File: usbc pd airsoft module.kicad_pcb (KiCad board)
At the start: 2 copper layers, 135 x 21 mm, 102 parts, among them J1 USB_C_Receptacle_USB2.0_16P, J2 BALANCE 3S (JST-XH 4P), Q1 2N7002, Q2 DMP3099L, Q3 2N7002, U1 CH224K, U2 TPD2E2U06DCK, U3 BQ25798RQMR, U4 BQ7692003PWR, U5 AP7381-33SA-7, U6 STM32F042F6P6

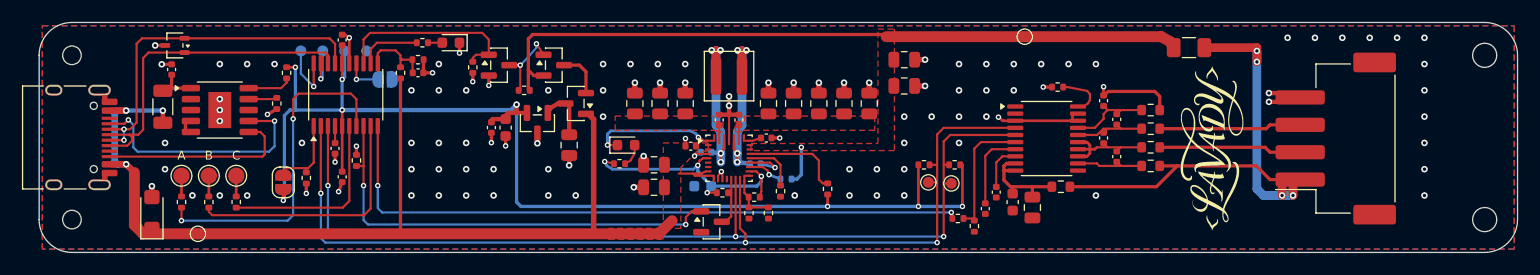
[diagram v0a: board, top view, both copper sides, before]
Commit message: Strap notches in both long edges, via-free back text, regenerated production files
- 4 U-notches (3.8 mm wide, 1.5 mm deep, rounded) at x 137.1 / 173.5, straight across
  from each other (21.0 mm centre to centre), so a strap can hold the 20.5 mm pack
  without sliding (layout_work/regionH.py).
- Copper kept >= 0.3 mm from the notches: bottom bus lanes packed upward (CHG_EN 117.9,
  SCL 118.45, SDA 119.0; I2C steps back down at the U3 tee-in), VBUS steps up past the
  x 137 notch, PWR_HOLD dips past it, R26/D4 to y 102.75, R23/C35 to y 106.3/107.3,
  BAT_P edge track dips at x 173.
- Back text '<desighned by Fluff>' moved by the user to x 125-152; vias kept off it
  (no stitching there, U6 fan-out vias to y 116.0, C29/C32/C34 GND vias moved).
- DRC 0 errors / 0 unconnected / schematic parity 0.
- Gerbers, drill, BOM, pick-and-place, assembly PDFs and zips regenerated.

Co-Authored-By: Claude Opus 5.5 <noreply@anthropic.com>
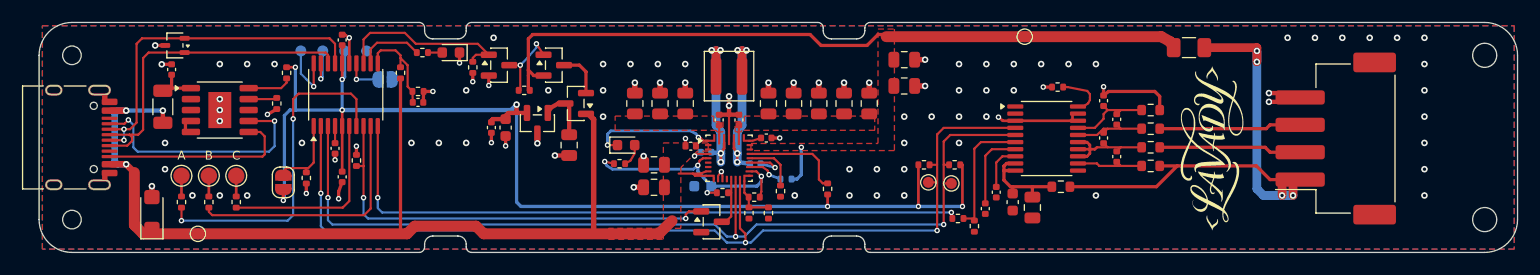
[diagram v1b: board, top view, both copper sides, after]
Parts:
- moved R23 2.90 mm to (134.6, 106.3)
- moved C35 2.70 mm to (134.6, 107.3)
- moved D4 0.90 mm to (137.6, 102.8)
- moved R26 0.90 mm to (135.0, 102.8)
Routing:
- net /VBUS_SENSE: track 6.14 -> 8.28 mm
- net /I2C_SDA: track 90.0 -> 88.7 mm
- net /I2C_SCL: track 86.6 -> 85.3 mm
- net /CHG_EN: track 40.5 -> 39.6 mm
- net /BAT_P: track 69.5 -> 70.3 mm
- net /PWR_HOLD: track 16.9 -> 16.0 mm
- net /GND: track 55.5 -> 56.1 mm, vias 111 -> 98
- net /VBUS: track 98.6 -> 99.2 mm
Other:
- outline, holes or cut-outs redrawn
- board text added: "fast charging"
- board text removed: "CELL MONITOR BQ76920"
- board text removed: "CHARGER BQ25798"
- board text removed: "CONNECTORS (place these first)"
- board text removed: "MCU"
- board text removed: "MCU POWER"
- board text removed: "USB-C / PD"
